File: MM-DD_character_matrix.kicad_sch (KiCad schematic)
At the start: 14 parts, among them U15 SN74LVC244A, U16 SM411006N/15, U17 SM411006N/15, U18 SN74LVC244A, U19 SM411006N/15, U20 SM411006N/15, U21 SM411006N/15

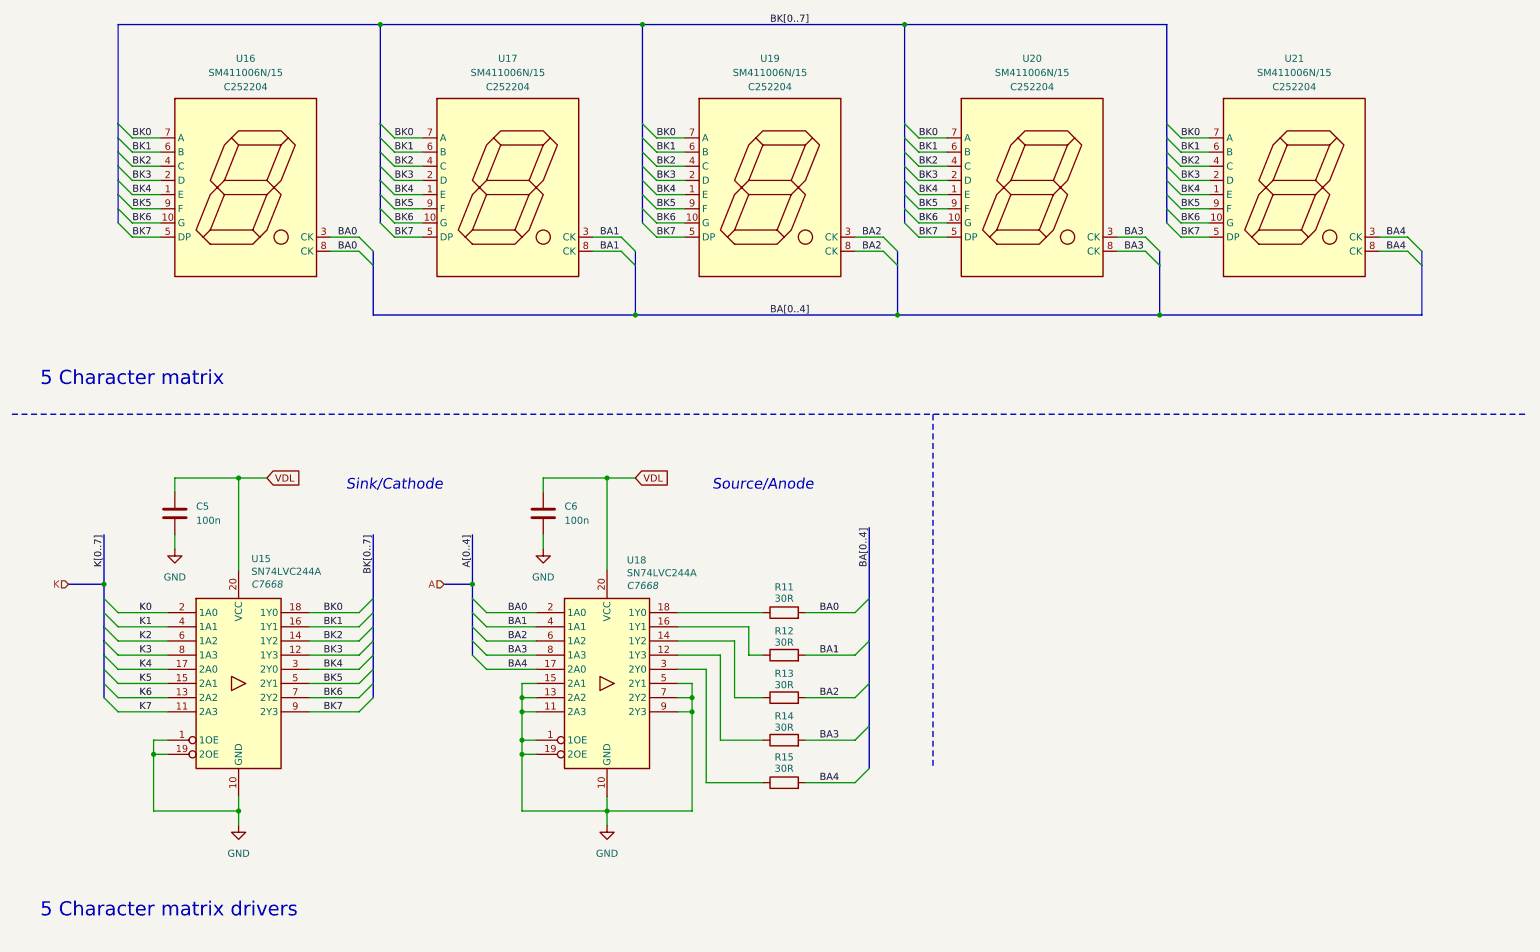
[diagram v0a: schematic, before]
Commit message: addition of bus
- cleaned up the structure of the schematic.
- addition of the colon
- root schematic improvements
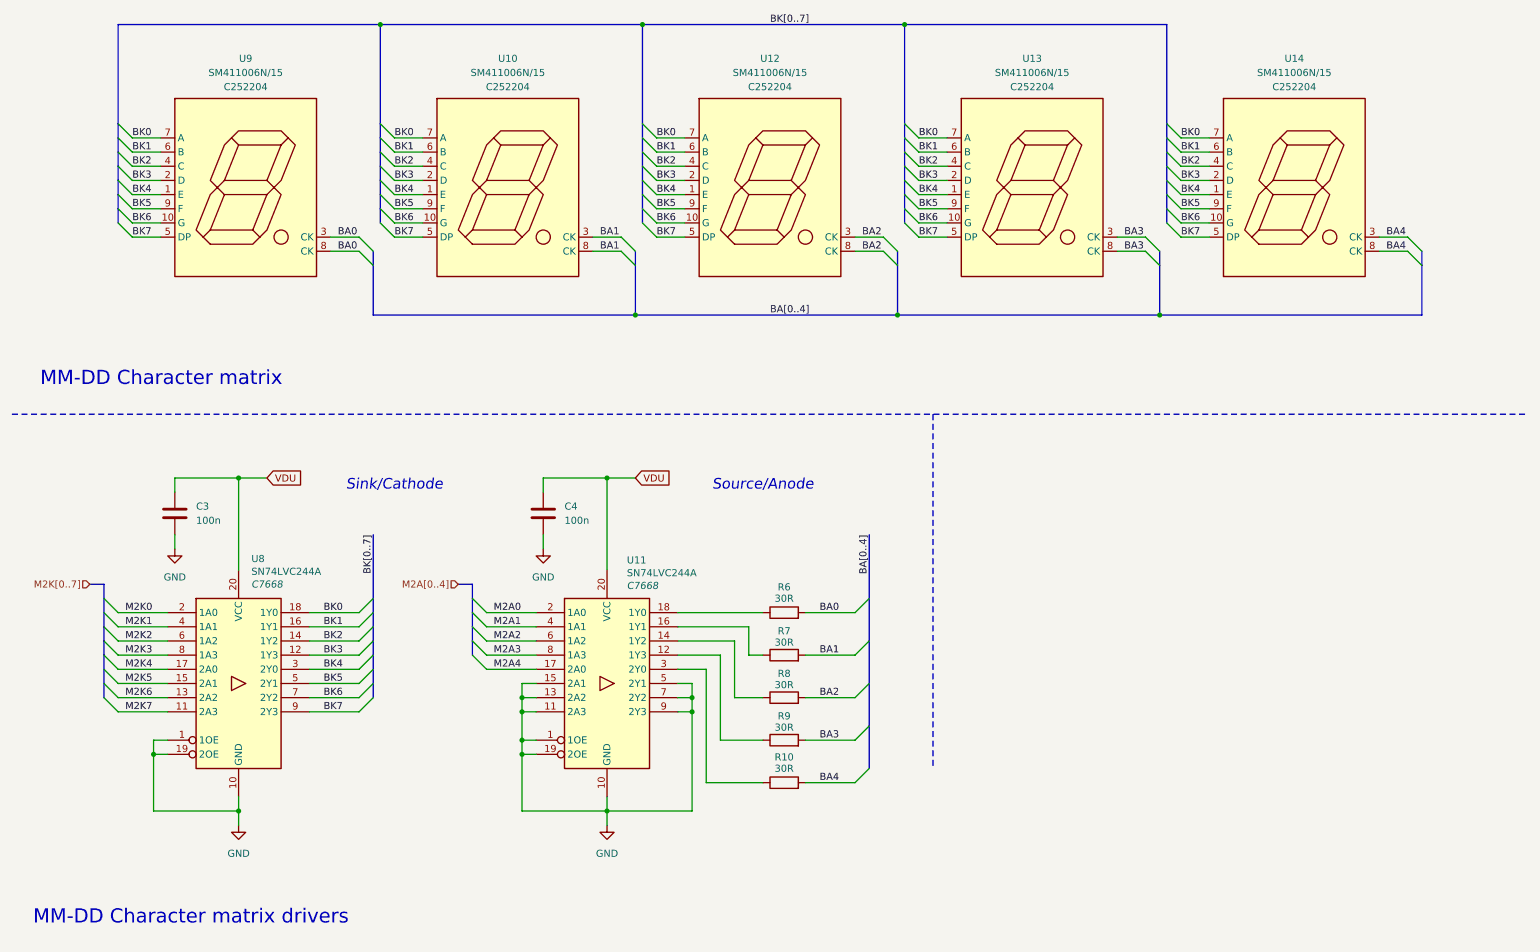
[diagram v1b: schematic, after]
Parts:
- removed C5, C6: 100n, symbol Device:C
- removed R11, R12, R13, R14, R15: 30R, symbol Device:R
- removed U15, U18: SN74LVC244A, Package_SO:TSSOP-20_4.4x6.5mm_P0.65mm, symbol 74xx:74AHC244
- removed U16, U17, U19, U20, U21: SM411006N/15, precision_clock:SM411006N15, symbol precision_clock:SM411006N/15
- added C3, C4: 100n, symbol Device:C
- added R10, R6, R7, R8, R9: 30R, symbol Device:R
- added U10, U12, U13, U14, U9: SM411006N/15, precision_clock:SM411006N15, symbol precision_clock:SM411006N/15
- added U11, U8: SN74LVC244A, Package_SO:TSSOP-20_4.4x6.5mm_P0.65mm, symbol 74xx:74AHC244
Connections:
- net BA0: now also R6.2, U9.3 (CK), U9.8 (CK)
- net BA1: now also R7.2, U10.3 (CK), U10.8 (CK)
- net BA2: now also R8.2, U12.3 (CK), U12.8 (CK)
- net BA3: now also R9.2, U13.3 (CK), U13.8 (CK)
- net BA4: now also R10.2, U14.3 (CK), U14.8 (CK)
- net BK0: now also U10.7 (A), U12.7 (A), U13.7 (A), U14.7 (A), U8.18 (1Y0), U9.7 (A)
- net BK1: now also U10.6 (B), U12.6 (B), U13.6 (B), U14.6 (B), U8.16 (1Y1), U9.6 (B)
- net BK2: now also U10.4 (C), U12.4 (C), U13.4 (C), U14.4 (C), U8.14 (1Y2), U9.4 (C)
- net BK3: now also U10.2 (D), U12.2 (D), U13.2 (D), U14.2 (D), U8.12 (1Y3), U9.2 (D)
- net BK4: now also U10.1 (E), U12.1 (E), U13.1 (E), U14.1 (E), U8.3 (2Y0), U9.1 (E)
- net BK5: now also U10.9 (F), U12.9 (F), U13.9 (F), U14.9 (F), U8.5 (2Y1), U9.9 (F)
- net BK6: now also U10.10 (G), U12.10 (G), U13.10 (G), U14.10 (G), U8.7 (2Y2), U9.10 (G)
- net BK7: now also U10.5 (DP), U12.5 (DP), U13.5 (DP), U14.5 (DP), U8.9 (2Y3), U9.5 (DP)
- net GND: now also C3.2, C4.2, U11.1 (1OE), U11.10 (GND), U11.11 (2A3), U11.13 (2A2), U11.15 (2A1), U11.19 (2OE), U11.5 (2Y1), U11.7 (2Y2), U11.9 (2Y3), U8.1 (1OE), U8.10 (GND), U8.19 (2OE)
- new net: R8.1, U11.14 (1Y2)
- new net: R9.1, U11.12 (1Y3)
- new net: R7.1, U11.16 (1Y1)
- new net: R6.1, U11.18 (1Y0)
- new net: R10.1, U11.3 (2Y0)
- new net M2A0: U11.2 (1A0)
- new net M2A1: U11.4 (1A1)
- new net M2A2: U11.6 (1A2)
- new net M2A3: U11.8 (1A3)
- new net M2A4: U11.17 (2A0)
- new net M2K0: U8.2 (1A0)
- new net M2K1: U8.4 (1A1)
- new net M2K2: U8.6 (1A2)
- new net M2K3: U8.8 (1A3)
- new net M2K4: U8.17 (2A0)
- new net M2K5: U8.15 (2A1)
- new net M2K6: U8.13 (2A2)
- new net M2K7: U8.11 (2A3)
- new net VDU: C3.1, C4.1, U11.20 (VCC), U8.20 (VCC)
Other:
- note added: "MM-DD Character matrix"
- note added: "MM-DD Character matrix drivers"
- note removed: "5 Character matrix"
- note removed: "5 Character matrix drivers"
- title: 5 Character Matrix & Drivers  -> MM-DD Character Matrix & Drivers 

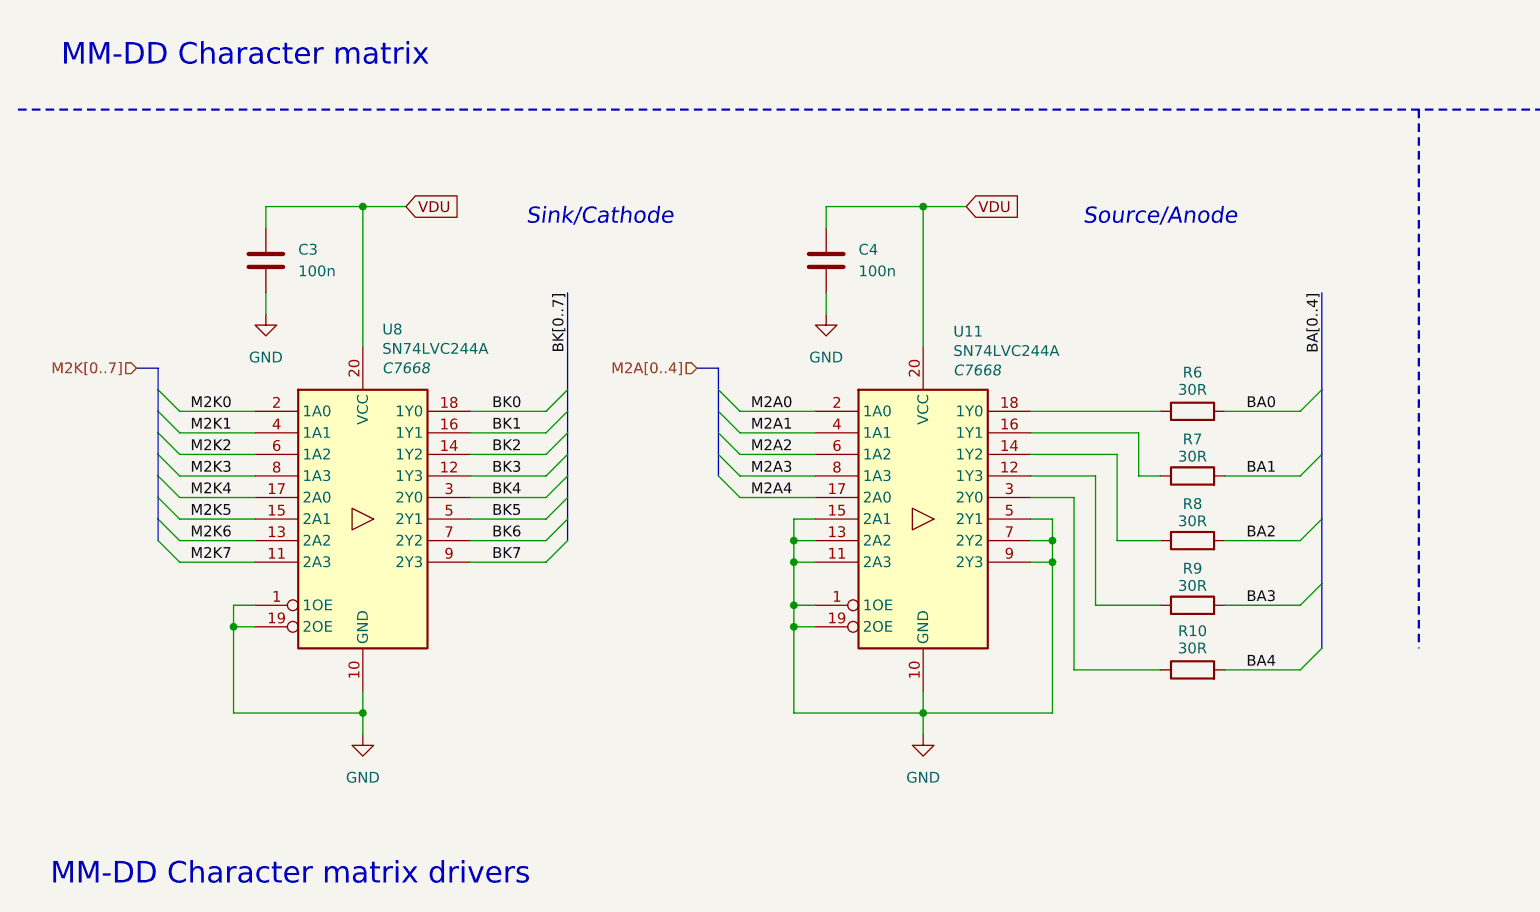
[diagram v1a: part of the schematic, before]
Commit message: current limiting resistor changes
- added colon led model, but might replace it in the future.
- reduction in current limiting resistance.
- removed the solder jumps in the individual circuit schematics.
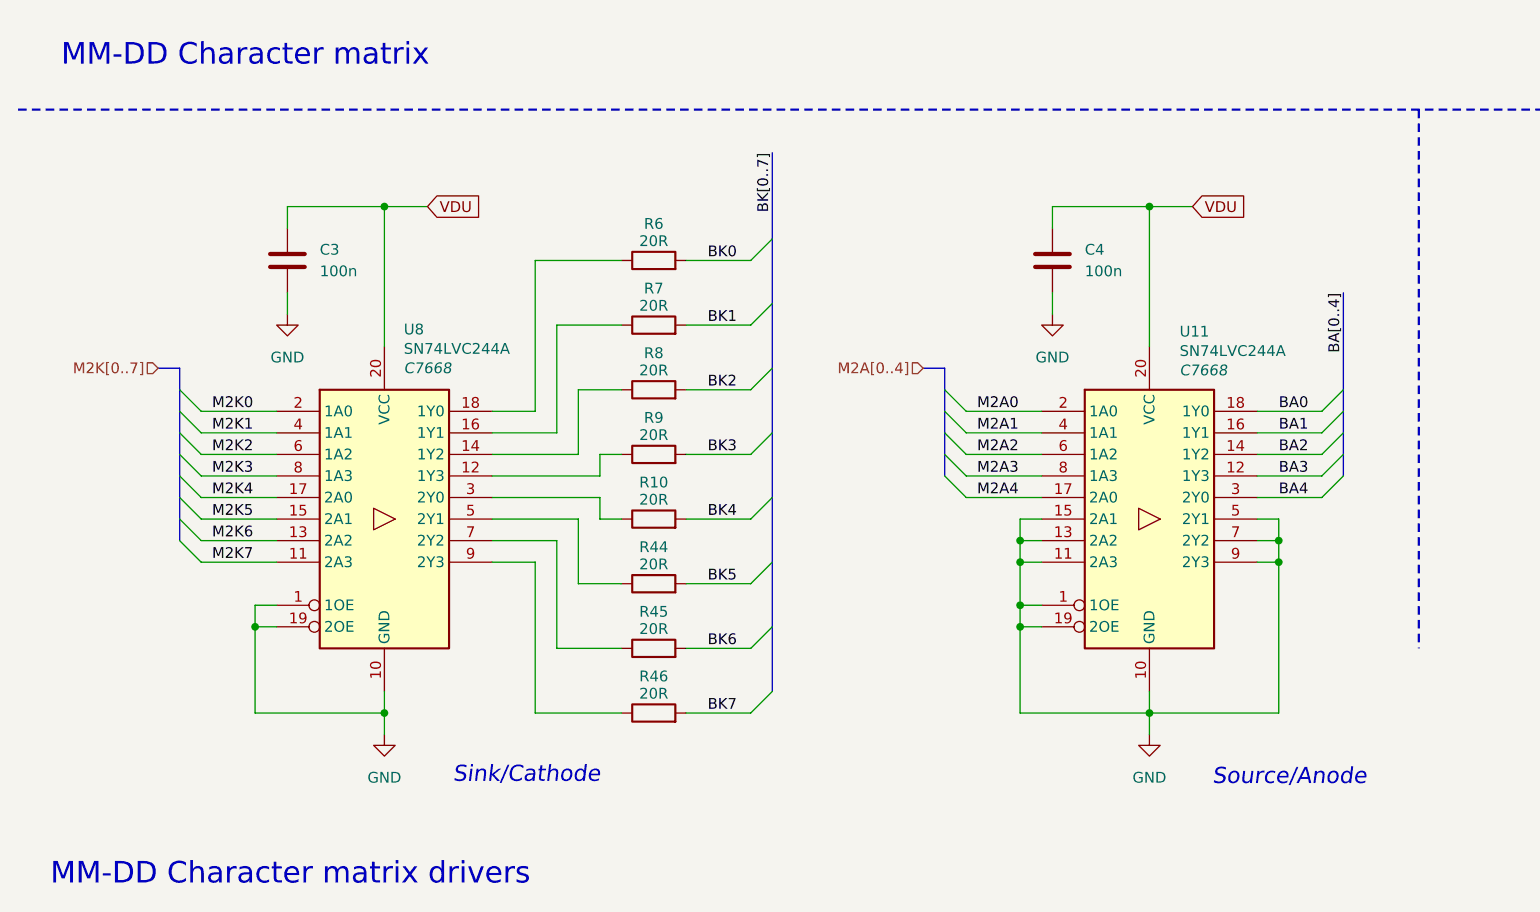
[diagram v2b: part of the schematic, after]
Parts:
- added R44, R45, R46: 20R, symbol Device:R
- R10, R6, R7, R8, R9: value 30R -> 20R
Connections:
- net BA0: now also U11.18 (1Y0); no longer R6.2
- net BA1: now also U11.16 (1Y1); no longer R7.2
- net BA2: now also U11.14 (1Y2); no longer R8.2
- net BA3: now also U11.12 (1Y3); no longer R9.2
- net BA4: now also U11.3 (2Y0); no longer R10.2
- net BK0: now also R6.2; no longer U8.18 (1Y0)
- net BK1: now also R7.2; no longer U8.16 (1Y1)
- net BK2: now also R8.2; no longer U8.14 (1Y2)
- net BK3: now also R9.2; no longer U8.12 (1Y3)
- net BK4: now also R10.2; no longer U8.3 (2Y0)
- net BK5: now also R44.2; no longer U8.5 (2Y1)
- net BK6: now also R45.2; no longer U8.7 (2Y2)
- net BK7: now also R46.2; no longer U8.9 (2Y3)
- net at R8.1: now also U8.14 (1Y2); no longer U11.14 (1Y2)
- net at R9.1: now also U8.12 (1Y3); no longer U11.12 (1Y3)
- net at R7.1: now also U8.16 (1Y1); no longer U11.16 (1Y1)
- net at R6.1: now also U8.18 (1Y0); no longer U11.18 (1Y0)
- net at R10.1: now also U8.3 (2Y0); no longer U11.3 (2Y0)
- new net: R44.1, U8.5 (2Y1)
- new net: R45.1, U8.7 (2Y2)
- new net: R46.1, U8.9 (2Y3)
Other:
- moved on the sheet: C3, C4, U11, U8

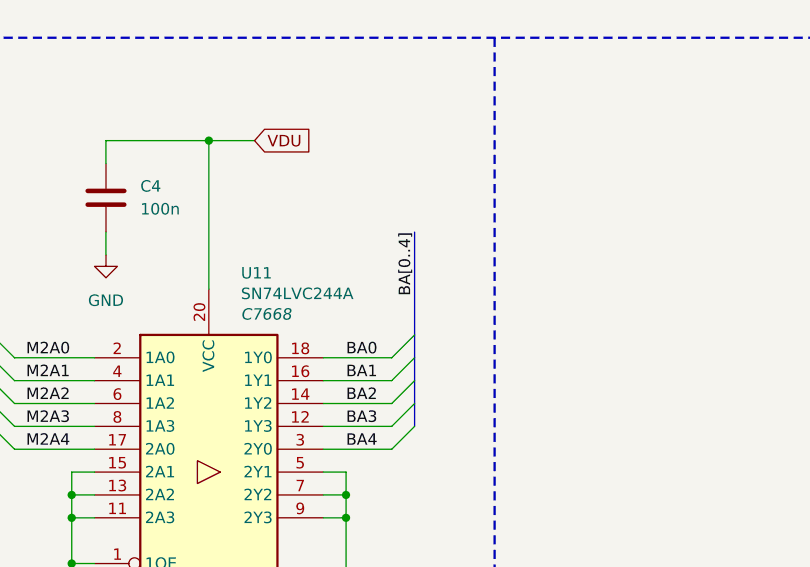
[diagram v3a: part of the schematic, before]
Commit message: Buzzer driver added - replacement of photoresistor to a variable resistor - added button - general formatting
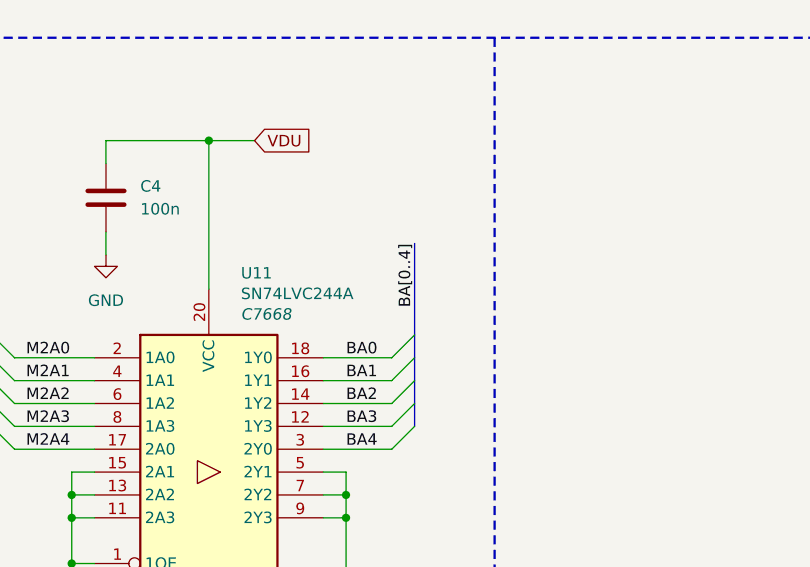
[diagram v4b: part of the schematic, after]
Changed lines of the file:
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@@
 	(bus
 		(pts
-			(xy 168.91 123.19) (xy 168.91 134.62)
+			(xy 168.91 124.46) (xy 168.91 134.62)
 		)
 		(stroke
@@
 	)
 	(label "BA[0..4]"
-		(at 168.91 123.19 270)
-		(effects
-			(font
+		(at 168.91 124.46 270)
+		(effects
+			(font

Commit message: ESD, LEDs, footprints
- assignment of footprints
- ESD protection
- User buttons
- addition of test points
- BOM consolidation of  resistors
- general reordering of the schematic
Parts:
- C3, C4: footprint (none) -> Capacitor_SMD:C_0603_1608Metric
- R10, R44, R45, R46, R6, R7, R8, R9: footprint (none) -> Resistor_SMD:R_0603_1608Metric
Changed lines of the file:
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@@
 	(title_block
 		(title "MM-DD Character Matrix & Drivers ")
-		(date "2025-10-31")
+		(date "2025-11-04")
 		(rev "v0.0")
 		(company "Rajath Katker")
@@
 			)
 		)
-		(property "Footprint" ""
+		(property "Footprint" "Capacitor_SMD:C_0603_1608Metric"
 			(at 45.4152 123.19 0)
 			(effects
@@
 			)
 		)
-		(property "Footprint" ""
+		(property "Footprint" "Resistor_SMD:R_0603_1608Metric"
 			(at 87.63 174.498 90)
 			(effects
@@
 			)
 		)
-		(property "Footprint" ""
+		(property "Footprint" "Resistor_SMD:R_0603_1608Metric"
 			(at 87.63 151.638 90)
 			(effects
@@
 			)
 		)
-		(property "Footprint" ""
+		(property "Footprint" "Resistor_SMD:R_0603_1608Metric"
 			(at 87.63 166.878 90)
 			(effects
@@
 			)
 		)
-		(property "Footprint" ""
+		(property "Footprint" "Resistor_SMD:R_0603_1608Metric"
 			(at 87.63 159.258 90)
 			(effects
@@
 			)
 		)
-		(property "Footprint" ""
+		(property "Footprint" "Capacitor_SMD:C_0603_1608Metric"
 			(at 135.5852 123.19 0)
 			(effects
@@
 			)
 		)
-		(property "Footprint" ""
+		(property "Footprint" "Resistor_SMD:R_0603_1608Metric"
 			(at 87.63 121.158 90)
 			(effects
@@
 			)
 		)
-		(property "Footprint" ""
+		(property "Footprint" "Resistor_SMD:R_0603_1608Metric"
 			(at 87.63 136.398 90)
 			(effects
@@
 			)
 		)
-		(property "Footprint" ""
+		(property "Footprint" "Resistor_SMD:R_0603_1608Metric"
 			(at 87.63 128.778 90)
 			(effects
@@
 			)
 		)
-		(property "Footprint" ""
+		(property "Footprint" "Resistor_SMD:R_0603_1608Metric"
 			(at 87.63 144.018 90)
 			(effects
